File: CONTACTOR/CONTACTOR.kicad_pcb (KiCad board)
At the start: 4 copper layers, 96.5 x 96.5 mm, 0 parts

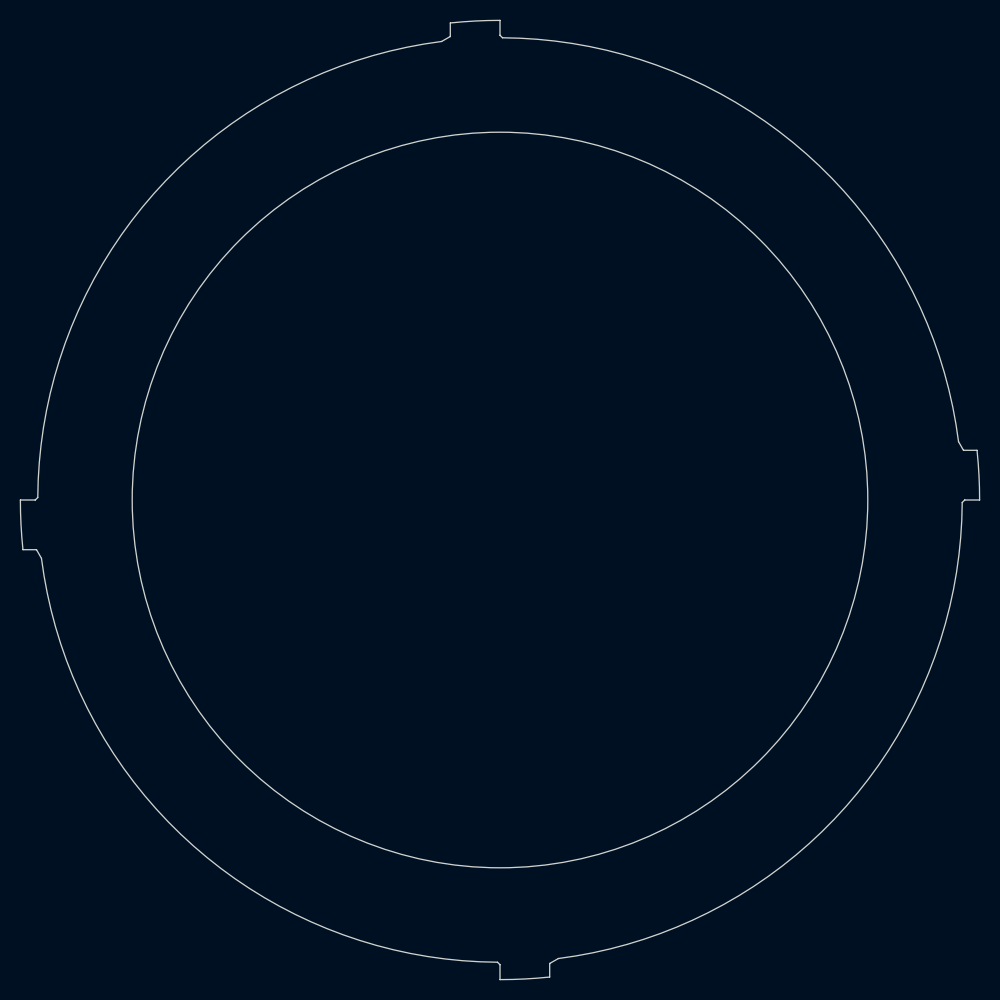
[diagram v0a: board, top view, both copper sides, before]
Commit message: Update designation.
Update CONTACTOR and RAIL.
Add INNER_HOLDER.
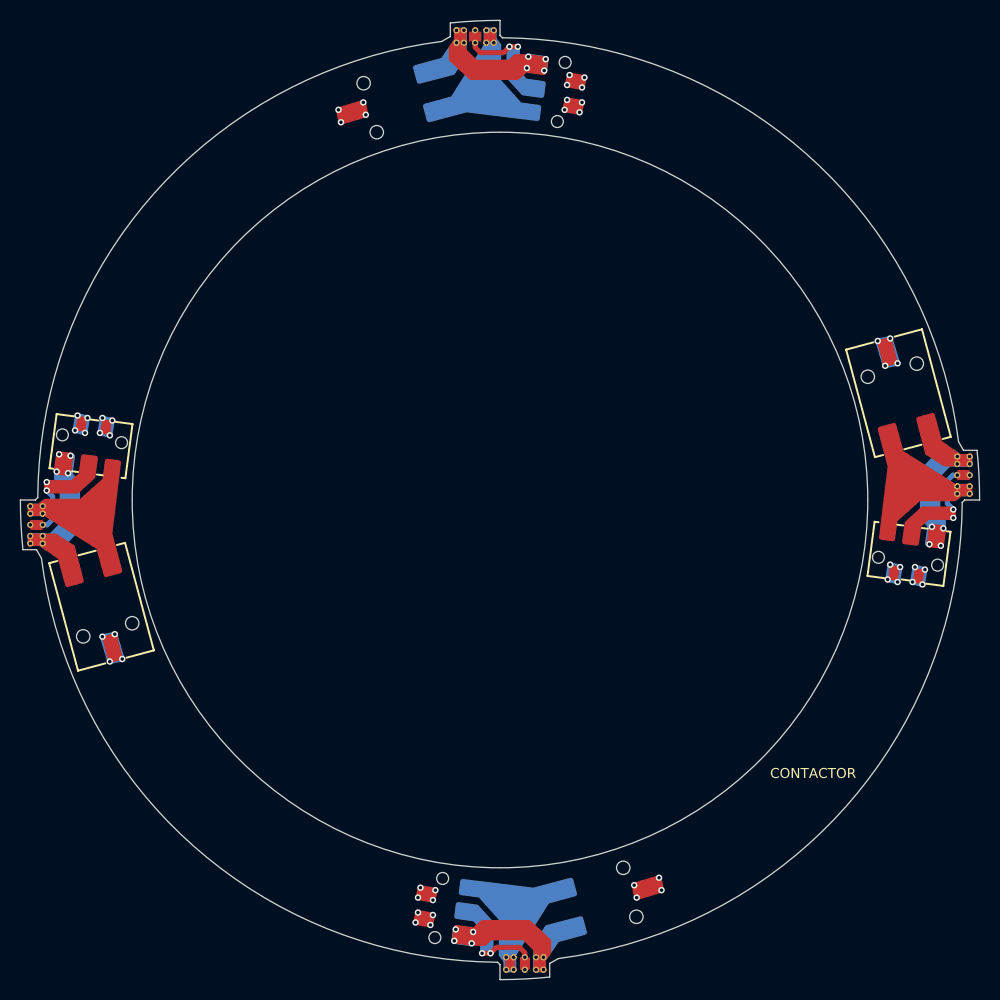
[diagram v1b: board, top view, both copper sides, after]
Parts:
- added CONTACTOR: ESR_CONTACTOR, MECHANICAL:ESR_CONTACTOR, F.Cu at (100.0, 100.0)
- added REF**: BC-1107_2, GENERAL_CONNECTOR_SMD:BC-1107_2, F.Cu at (140.1, 89.3)
- added REF**: BC-0705_3, GENERAL_CONNECTOR_SMD:BC-0705_3, F.Cu at (141.1, 105.4)
- added REF**: BC-1107_2, GENERAL_CONNECTOR_SMD:BC-1107_2, B.Cu at (89.3, 59.9)
- added REF**2: BC-0705_3, GENERAL_CONNECTOR_SMD:BC-0705_3, B.Cu at (105.4, 58.9)
- added REF**3: BC-1107_2, GENERAL_CONNECTOR_SMD:BC-1107_2, F.Cu at (59.9, 110.7)
- added REF**4: BC-0705_3, GENERAL_CONNECTOR_SMD:BC-0705_3, F.Cu at (58.9, 94.6)
- added REF**5: BC-0705_3, GENERAL_CONNECTOR_SMD:BC-0705_3, B.Cu at (94.6, 141.1)
- added REF**6: BC-1107_2, GENERAL_CONNECTOR_SMD:BC-1107_2, B.Cu at (110.7, 140.1)
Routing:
- net (no net): track 0.00 -> 20.9 mm, vias 0 -> 72
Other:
- outline, holes or cut-outs redrawn
- copper layers 4 -> 2
